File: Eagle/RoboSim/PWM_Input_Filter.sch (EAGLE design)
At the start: 66 parts, among them IC1 TLV2772, IC2 TLV2772, IC3 TLV2772

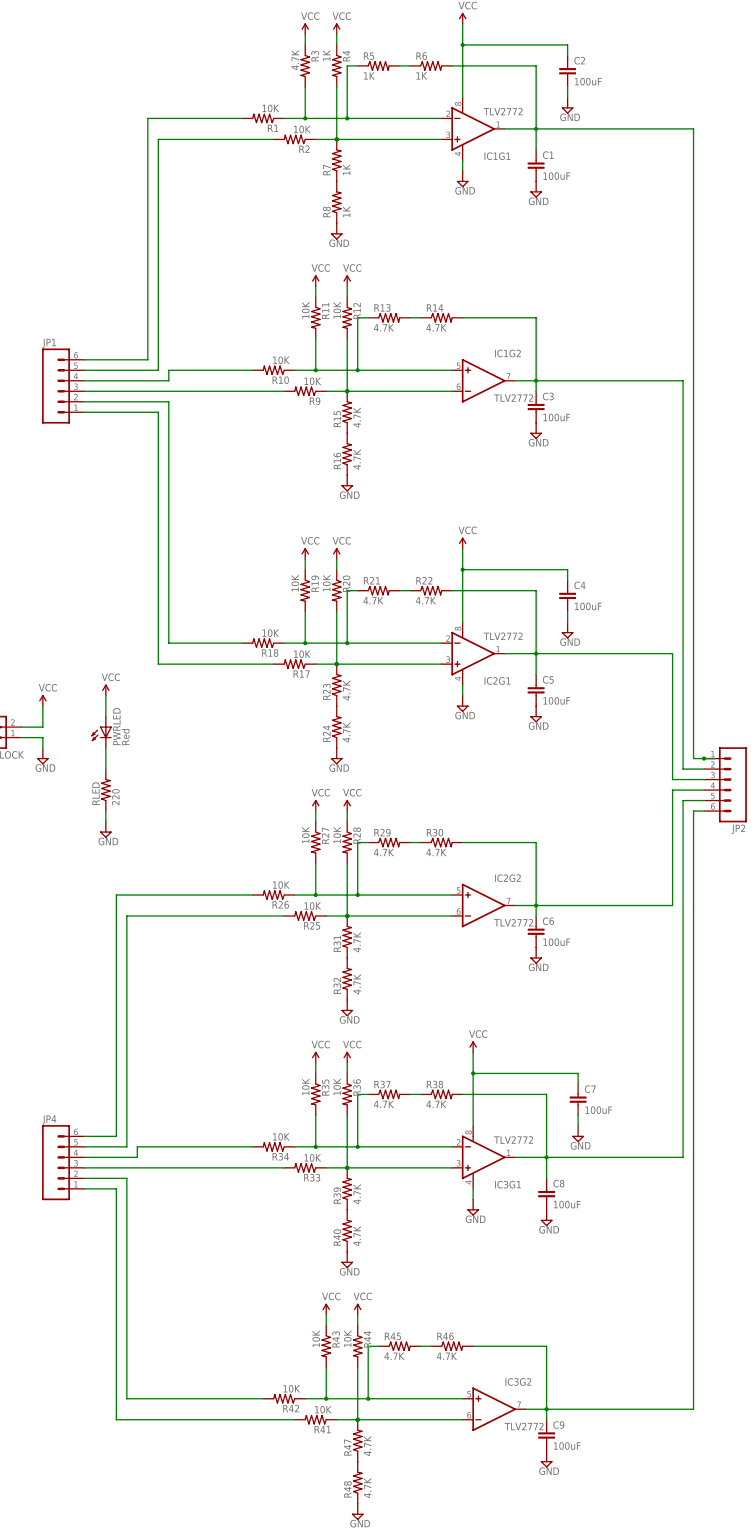
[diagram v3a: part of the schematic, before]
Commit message: updated resistor values and op-amp configuration
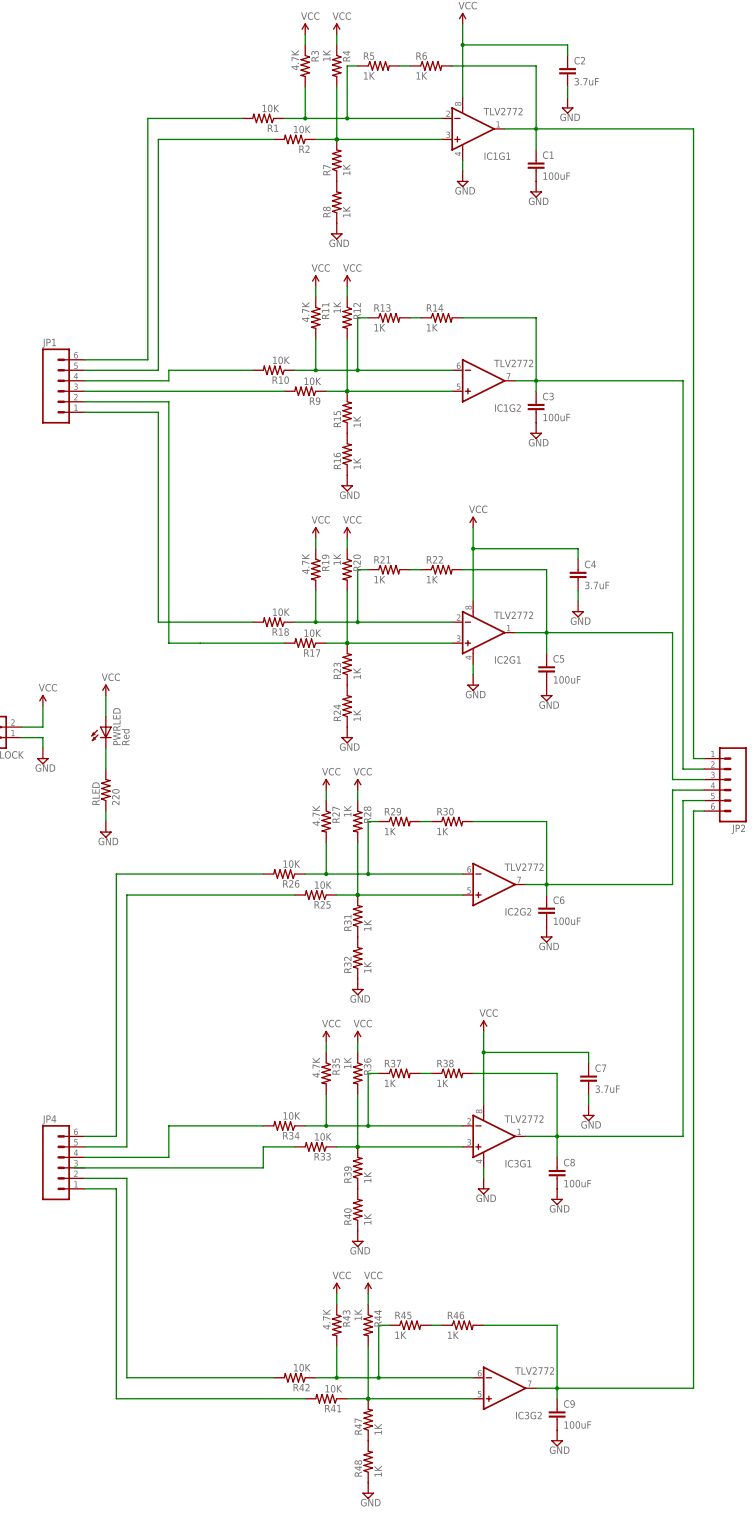
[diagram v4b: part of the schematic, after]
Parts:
- C2, C4, C7: value 100uF -> 3.7uF
- R11, R19, R27, R35, R43: value 10K -> 4.7K
- R12, R20, R28, R36, R44: value 10K -> 1K
- R13, R14, R15, R16, R21, R22, R23, R24, R29, R30, R31, R32, R37, R38, R39, R40, R45, R46, R47, R48: value 4.7K -> 1K
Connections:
- removed net N$26 (its old number): IC2G2.+IN, R26.1, R27.2, R29.1
- removed net N$27 (its old number): IC2G2.-IN, R25.1, R28.2, R31.2
- removed net N$32 (its old number): JP4.3, R33.2
- removed net N$40 (its old number): IC3G2.+IN, R42.1, R43.2, R45.1
- removed net N$41 (its old number): IC3G2.-IN, R41.1, R44.2, R47.2
- new net N$28: IC2G2.-IN, R26.1, R27.2, R29.1
- new net N$29: IC2G2.+IN, R25.1, R28.2, R31.2
- new net N$31: R33.2
- new net N$48: IC3G2.-IN, R42.1, R43.2, R45.1
- new net N$49: IC3G2.+IN, R41.1, R44.2, R47.2
- net N$11: now also IC1G2.-IN; no longer IC1G2.+IN
- net N$12: now also IC1G2.+IN; no longer IC1G2.-IN
- net N$16: now also R18.2; no longer R17.2
- net N$2: now also R17.2; no longer R18.2
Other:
- moved on the sheet: C4, C5, C6, C7, C8, C9, IC1G2, IC2G1, IC2G2, IC3G1, IC3G2, R17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

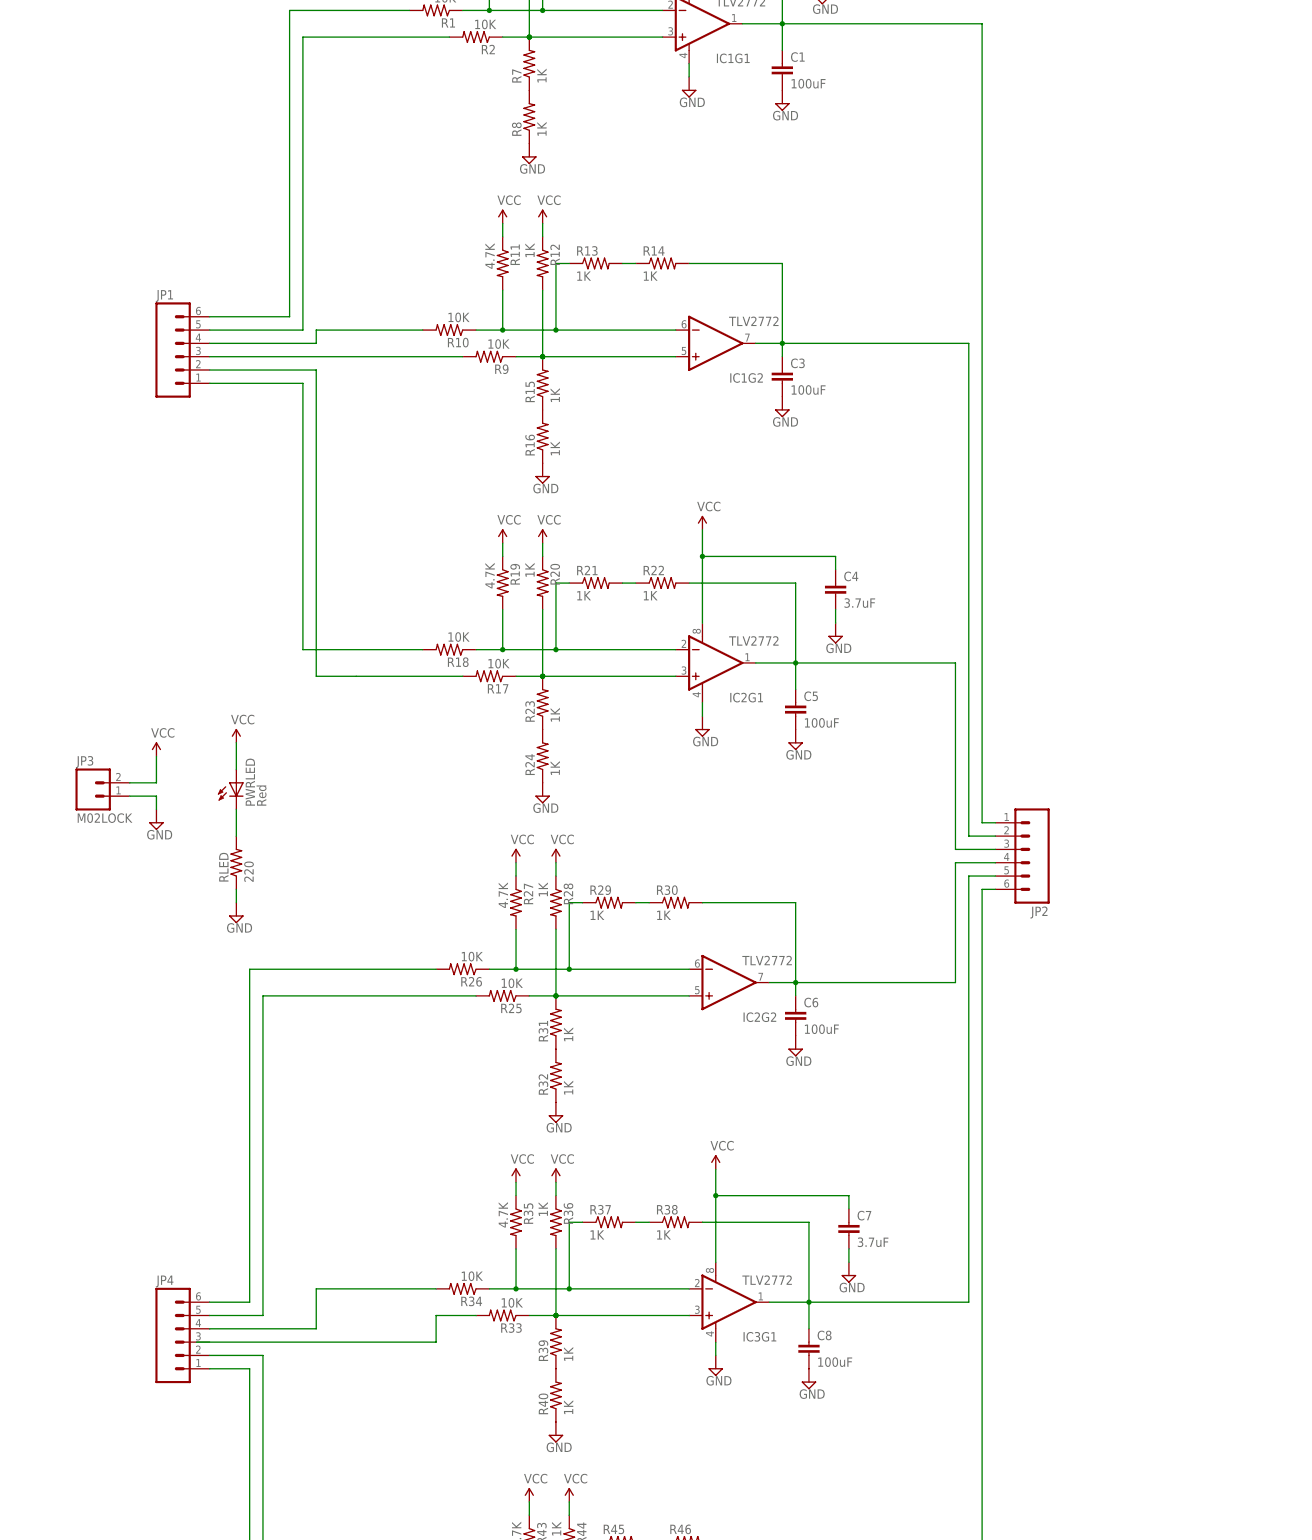
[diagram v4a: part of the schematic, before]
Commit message: changed pins to screw terminals and made resistors surface mount. Still need to position components and route
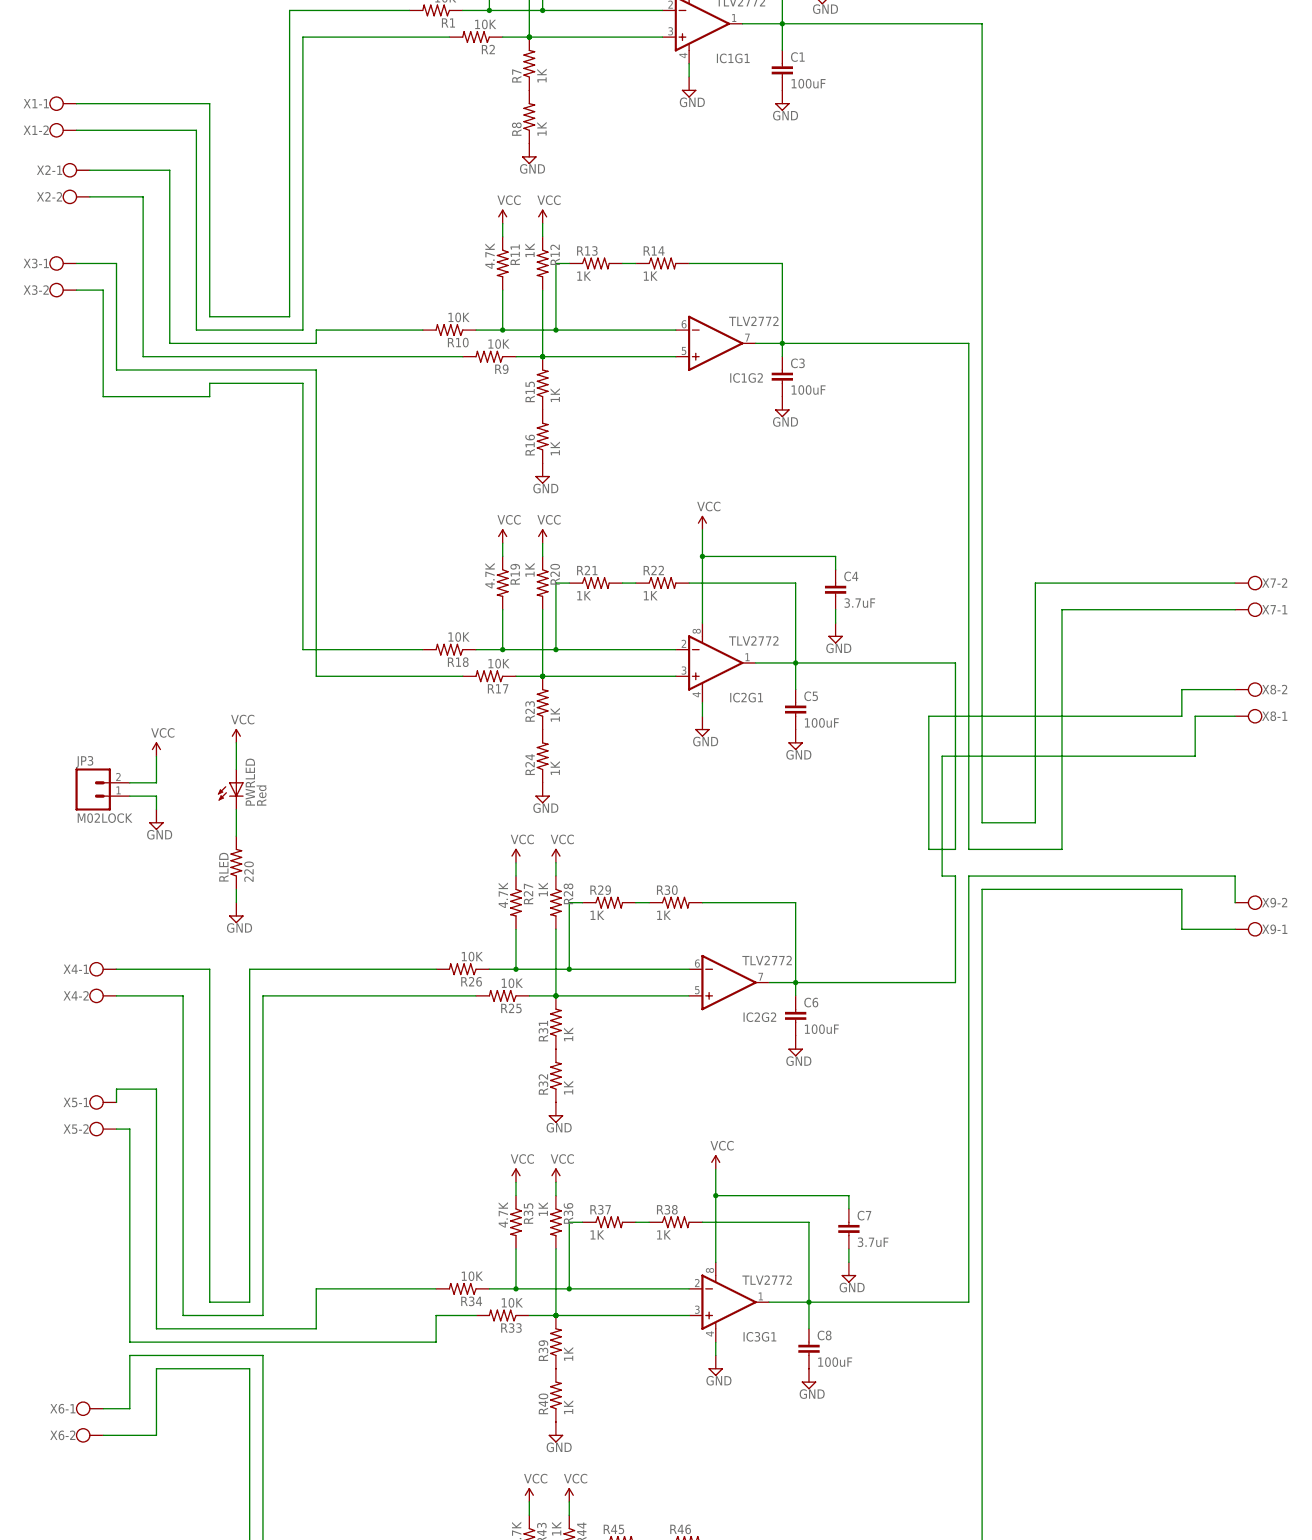
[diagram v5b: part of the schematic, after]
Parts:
- removed JP1, JP2, JP4: (no value), SparkFun-Connectors:M06LOCK
- added X1, X2, X3, X4, X5, X6, X7, X8, X9: (no value), con-wago-500:W237-102
- R1, R10, R11, R12, R13, R14, R15, R16, R17, R18, R19, R2, R20, R21, R22, R23, R24, R25, R26, R27, R28, R29, R3, R30, R31, R32, R33, R34, R35, R36, R37, R38, R39, R4, R40, R41, R42, R43, R44, R45, R46, R47, R48, R5, R6, R7, R8, R9, RLED: device SparkFun-Passives:RESISTORPTH-1/4W -> SparkFun-Passives:RESISTOR1206
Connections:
- removed net N$42: JP4.1, R41.2
- new net N$34: R41.2, X6-2.KL
- net N$1: now also X1-1.KL; no longer JP1.6
- net N$13: now also X7-1.KL; no longer JP2.2
- net N$14: now also X2-1.KL; no longer JP1.4
- net N$16: now also X3-2.KL; no longer JP1.1
- net N$18: now also X8-1.KL; no longer JP2.4
- net N$2: now also X3-1.KL; no longer JP1.2
- net N$20: now also X4-2.KL; no longer JP4.5
- net N$21: now also X2-2.KL; no longer JP1.3
- net N$22: now also X4-1.KL; no longer JP4.6
- net N$30: now also X5-1.KL; no longer JP4.4
- net N$31: now also X5-2.KL
- net N$37: now also X8-2.KL; no longer JP2.3
- net N$40: now also X9-1.KL; no longer JP2.6
- net N$41: now also X6-1.KL; no longer JP4.2
- net N$44: now also X7-2.KL; no longer JP2.1
- net N$52: now also X9-2.KL; no longer JP2.5
- net N$8: now also X1-2.KL; no longer JP1.5
